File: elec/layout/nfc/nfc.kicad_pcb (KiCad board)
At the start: 2 copper layers, 40 x 40 mm, 0 parts

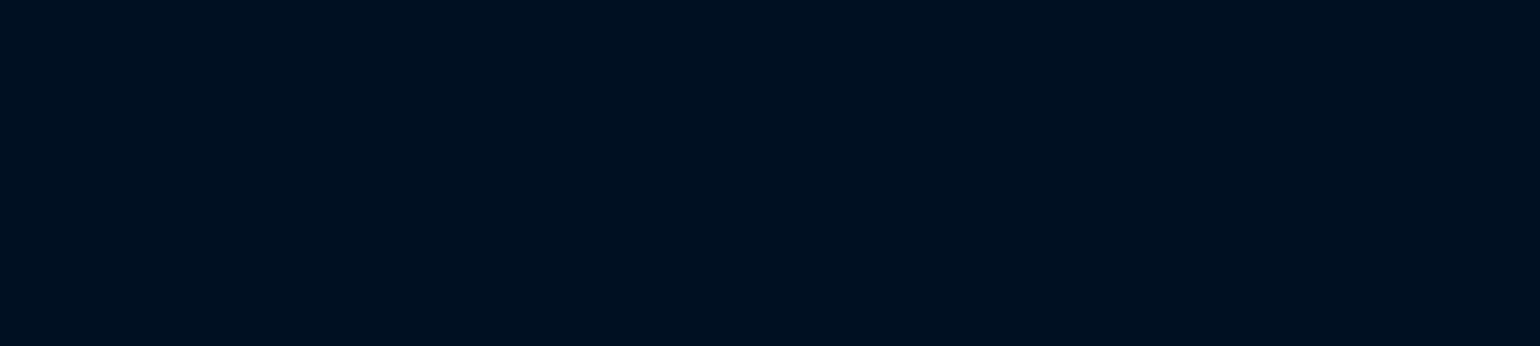
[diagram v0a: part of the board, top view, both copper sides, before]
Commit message: import copper features to hat board
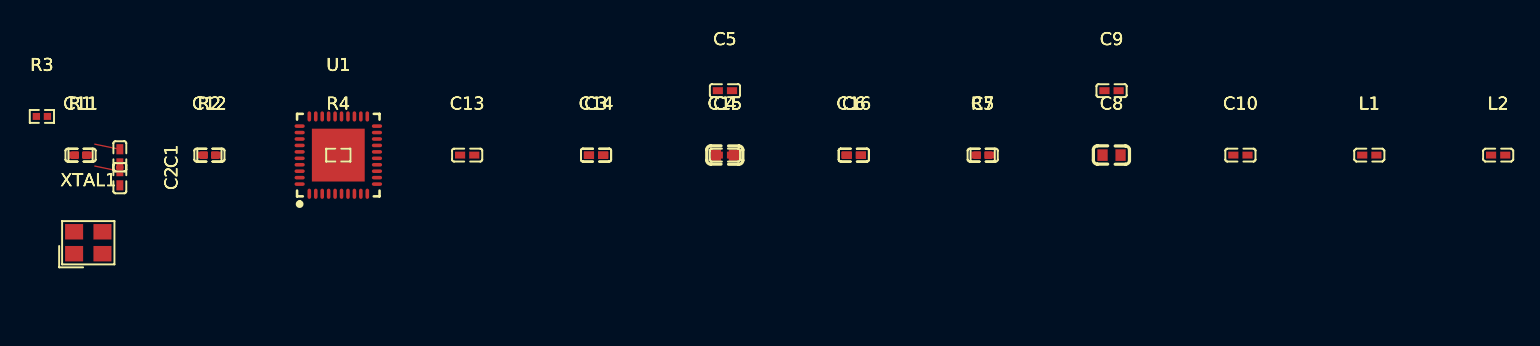
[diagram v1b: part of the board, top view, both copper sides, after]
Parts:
- added C1: , lcsc:C0402, F.Cu at (96.5, 59.7)
- added C10: , lcsc:C0402, F.Cu at (183.4, 59.6)
- added C11: 100nF ±10% 16V X7R, lcsc:C0402, F.Cu at (93.4, 59.6)
- added C12: , lcsc:C0402, F.Cu at (103.4, 59.6)
- added C13: , lcsc:C0402, F.Cu at (123.4, 59.6)
- added C14, C3: , lcsc:C0402, F.Cu at (133.4, 59.6)
- added C15: , lcsc:C0402, F.Cu at (143.4, 59.6)
- added C16, C6: , lcsc:C0402, F.Cu at (153.4, 59.6)
- added C2: , lcsc:C0402, F.Cu at (96.5, 61.4)
- added C4: 10µF ±10% 10V X5R, lcsc:C0603, F.Cu at (143.4, 59.6)
- added C5: , lcsc:C0402, F.Cu at (143.4, 54.6)
- added C7: , lcsc:C0402, F.Cu at (163.4, 59.6)
- added C8: , lcsc:C0603, F.Cu at (173.4, 59.6)
- added C9: , lcsc:C0402, F.Cu at (173.4, 54.6)
- added L1: 15nH ±5% 300mA 500mΩ, lcsc:L0402, F.Cu at (193.4, 59.6)
- added L2: , lcsc:L0402, F.Cu at (203.4, 59.6)
- added R1: 10Ω ±1% 62.5mW, lcsc:R0402, F.Cu at (93.4, 59.6)
- added R2: , lcsc:R0402, F.Cu at (103.4, 59.6)
- added R3: , lcsc:R0402, F.Cu at (90.4, 56.6)
- added R4: , lcsc:R0402, F.Cu at (113.4, 59.6)
- added R5: , lcsc:R0402, F.Cu at (163.4, 59.6)
- added U1: _NXP_Semicon_PN5321A3HN_C106_51, lcsc:QFN-40_L6.0-W6.0-P0.50-BL-EP4.1, F.Cu at (113.4, 59.6)
- added XTAL1: Crystal, lcsc:CRYSTAL-SMD_4P-L3.2-W2.5-BL, F.Cu at (94.0, 66.4)
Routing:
- net oscillator-net: track 0.00 -> 1.99 mm
- net net-6: track 0.00 -> 1.99 mm

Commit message: 50% layout for hat
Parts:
- moved C1 76.7 mm to (167.7, 88.1)
- moved C2 76.7 mm to (167.7, 89.8)
- moved C11 76.7 mm to (164.6, 88.0)
- moved R1 76.7 mm to (164.6, 88.0)
- moved R3 76.7 mm to (161.6, 85.0)
- moved XTAL1 63.9 mm to (152.6, 92.0), turned to -90 degrees
- moved U1 44.1 mm to (143.6, 91.8)
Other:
- board outline removed
- board text removed: "{{GITHASH}}"
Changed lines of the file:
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@@
 	(footprint "lcsc:C0402"
 		(layer "F.Cu")
-		(at 96.45 61.395 -90)
+		(at 167.65 89.795 -90)
 		(property "Reference" "C2"
 			(at 0 -4 -90)
@@
 	(footprint "lcsc:C0402"
 		(layer "F.Cu")
-		(at 96.45 59.695 -90)
+		(at 167.65 88.095 -90)
 		(property "Reference" "C1"
 			(at 0 -4 -90)
@@
 	(footprint "lcsc:QFN-40_L6.0-W6.0-P0.50-BL-EP4.1"
 		(layer "F.Cu")
-		(at 113.4 59.6)
+		(at 143.6 91.8)
 		(property "Reference" "U1"
 			(at 0 -7 0)
@@
 	(footprint "lcsc:R0402"
 		(layer "F.Cu")
-		(at 93.4 59.6)
+		(at 164.6 88)
 		(property "Reference" "R1"
 			(at 0 -4 0)
@@
 	(footprint "lcsc:CRYSTAL-SMD_4P-L3.2-W2.5-BL"
 		(layer "F.Cu")
-		(at 94 66.4)
+		(at 152.6 92 -90)
 		(property "Reference" "XTAL1"
-			(at 0 -4.85 0)
+			(at 0 -4.85 90)
 			(layer "F.SilkS")
 			(effects
@@
 		)
 		(property "Value" "Crystal"
-			(at 0 4.85 0)
+			(at 0 4.85 90)
 			(layer "F.Fab")
 			(effects
@@
 		)
 		(property "Footprint" ""
-			(at 0 0 0)
+			(at 0 0 90)
 			(layer "F.Fab")
 			(hide yes)
@@
 		)
 		(property "Datasheet" ""
-			(at 0 0 0)
+			(at 0 0 90)
 			(layer "F.Fab")
 			(hide yes)
@@
 		)
 		(property "Description" ""
-			(at 0 0 0)
+			(at 0 0 90)
 			(layer "F.Fab")
 			(hide yes)
@@
 		)
 		(property "atopile_address" "oscillator.crystal"
-			(at 0 0 0)
+			(at 0 0 90)
 			(layer "User.9")
 			(hide yes)
@@
 		)
 		(property "LCSC" "C70591"
-			(at 0 0 0)
+			(at 0 0 90)
 			(layer "User.9")
 			(hide yes)
@@
 		(attr smd)
 		(fp_line
-			(start -2.26 0.25)
-			(end -2.26 1.91)
+			(start -2.26 1.91)
+			(end -0.4 1.91)
 			(stroke
 				(width 0.15)
@@
 		)
 		(fp_line
-			(start -2.26 1.91)
-			(end -0.4 1.91)
+			(start -2.03 1.68)
+			(end -2.03 -1.68)
 			(stroke
 				(width 0.15)
@@
 		)
 		(fp_line
-			(start -2.03 -1.68)
-			(end 2.03 -1.68)
+			(start 2.03 1.68)
+			(end -2.03 1.68)
 			(stroke
 				(width 0.15)
@@
 		)
 		(fp_line
-			(start -2.03 1.68)
-			(end -2.03 -1.68)
+			(start -2.26 0.25)
+			(end -2.26 1.91)
 			(stroke
 				(width 0.15)
@@
 		)
 		(fp_line
-			(start 2.03 -1.68)
-			(end 2.03 1.68)
+			(start -2.03 -1.68)
+			(end 2.03 -1.68)
 			(stroke
 				(width 0.15)
@@
 		)
 		(fp_line
-			(start 2.03 1.68)
-			(end -2.03 1.68)
+			(start 2.03 -1.68)
+			(end 2.03 1.68)
 			(stroke
 				(width 0.15)
@@
 		)
 		(fp_text user "${REFERENCE}"
-			(at 0 -4.85 0)
+			(at 0 -4.85 90)
 			(layer "F.SilkS")
 			(effects
@@
 		)
 		(fp_text user "${REFERENCE}"
-			(at 0 0 0)
+			(at 0 0 90)
 			(layer "F.Fab")
 			(effects
@@
 		)
 		(fp_text user "FBRK:autoplaced"
-			(at 0 0 0)
+			(at 0 0 90)
 			(layer "User.5")
 			(effects
@@
 		)
 		(pad "1" smd rect
-			(at -1.1 0.85)
+			(at -1.1 0.85 270)
 			(size 1.4 1.2)
 			(layers "F.Cu" "F.Paste" "F.Mask")
@@
 		)
 		(pad "2" smd rect
-			(at 1.1 0.85)
+			(at 1.1 0.85 270)
 			(size 1.4 1.2)
 			(layers "F.Cu" "F.Paste" "F.Mask")
@@
 		)
 		(pad "3" smd rect
-			(at 1.1 -0.85)
+			(at 1.1 -0.85 270)
 			(size 1.4 1.2)
 			(layers "F.Cu" "F.Paste" "F.Mask")
@@
 		)
 		(pad "4" smd rect
-			(at -1.1 -0.85)
+			(at -1.1 -0.85 270)
 			(size 1.4 1.2)
 			(layers "F.Cu" "F.Paste" "F.Mask")
@@
 	(footprint "lcsc:C0402"
 		(layer "F.Cu")
-		(at 93.4 59.6)
+		(at 164.6 88)
 		(property "Reference" "C11"
 			(at 0 -4 0)
@@
 	(footprint "lcsc:R0402"
 		(layer "F.Cu")
-		(at 90.4 56.6)
+		(at 161.6 85)
 		(property "Reference" "R3"
 			(at 0 -4 0)
@@
 		)
 	)
-	(gr_circle
-		(center 133.352 82.11)
-		(end 135.052 82.11)
-		(stroke
-			(width 0.1)
-			(type solid)
-		)
-		(fill none)
-		(layer "Edge.Cuts")
-	)
-	(gr_circle
-		(center 165.352 114.11)
-		(end 167.052 114.11)
-		(stroke
-			(width 0.1)
-			(type solid)
-		)
-		(fill none)
-		(layer "Edge.Cuts")
-	)
-	(gr_circle
-		(center 165.352 82.11)
-		(end 167.052 82.11)
-		(stroke
-			(width 0.1)
-			(type solid)
-		)
-		(fill none)
-		(layer "Edge.Cuts")
-	)
-	(gr_arc
-		(start 169.352 114.11)
-		(mid 168.180427 116.938427)
-		(end 165.352 118.11)
-		(stroke
-			(width 0.1)
-			(type solid)
-		)
-		(layer "Edge.Cuts")
-	)
-	(gr_arc
-		(start 133.352 118.11)
-		(mid 130.523573 116.938427)
-		(end 129.352 114.11)
-		(stroke
-			(width 0.1)
-			(type solid)
-		)
-		(layer "Edge.Cuts")
-	)
-	(gr_line
-		(start 169.352 114.11)
-		(end 169.352 82.11)
-		(stroke
-			(width 0.1)
-			(type solid)
-		)
-		(layer "Edge.Cuts")
-	)
-	(gr_line
-		(start 129.352 82.11)
-		(end 129.352 114.11)
-		(stroke
-			(width 0.1)
-			(type solid)
-		)
-		(layer "Edge.Cuts")
-	)
-	(gr_arc
-		(start 165.352 78.11)
-		(mid 168.180427 79.281573)
-		(end 169.352 82.11)
-		(stroke
-			(width 0.1)
-			(type solid)
-		)
-		(layer "Edge.Cuts")
-	)
-	(gr_line
-		(start 165.352 78.11)
-		(end 133.352 78.11)
-		(stroke
-			(width 0.1)
-			(type solid)
-		)
-		(layer "Edge.Cuts")
-	)
-	(gr_arc
-		(start 129.352 82.11)
-		(mid 130.523573 79.281573)
-		(end 133.352 78.11)
-		(stroke
-			(width 0.1)
-			(type solid)
-		)
-		(layer "Edge.Cuts")
-	)
-	(gr_circle
-		(center 133.352 114.11)
-		(end 135.052 114.11)
-		(stroke
-			(width 0.1)
-			(type solid)
-		)
-		(fill none)
-		(layer "Edge.Cuts")
-	)
-	(gr_line
-		(start 133.352 118.11)
-		(end 165.352 118.11)
-		(stroke
-			(width 0.1)
-			(type solid)
-		)
-		(layer "Edge.Cuts")
-	)
-	(gr_text "{{GITHASH}}"
-		(at 140.240427 116.111573 0)
-		(layer "F.SilkS")
-		(effects
-			(font
-				(size 2 2)
-				(thickness 0.1)
-			)
-			(justify left bottom)
-		)
-	)
 	(segment
-		(start 96.45 59.15)
-		(end 94.5 58.75)
+		(start 167.65 87.55)
+		(end 165.7 87.15)
 		(width 0.1)
 		(layer "F.Cu")
@@
 	)
 	(segment
-		(start 96.45 60.85)
-		(end 94.5 60.45)
+		(start 167.65 89.25)
+		(end 165.7 88.85)
 		(width 0.1)
 		(layer "F.Cu")
 		(net 4)
 	)
-	(group ""
-		(members "019c0a6d-9bb8-42f8-8584-8f200b71a27b" "097c55d3-ce7a-4886-a7db-9a4e9fcd0127"
-			"0e8e5788-23b0-4e0e-993f-a94957498ae3" "178364bc-250e-4a39-b0ba-4262bbac4b46"
-			"3d8baf97-c836-4397-867c-23e52ff05ce1" "871dfad9-a85d-42ce-9d2d-6520fae7f4c4"
-			"8baef1cd-8e58-474a-b843-199aa0080763" "a7e36be5-cc10-4aad-836f-bde309666136"
-			"b80e33ff-046b-4986-bc0d-6bc4865afc31" "cf226ff4-3173-434d-8c9b-3129470c1ce4"
-			"d6648504-8f45-4127-8704-34acfec9c9a4" "e1f36007-0f9d-4dc5-ae43-6b056652526f"
-		)
-	)
 )

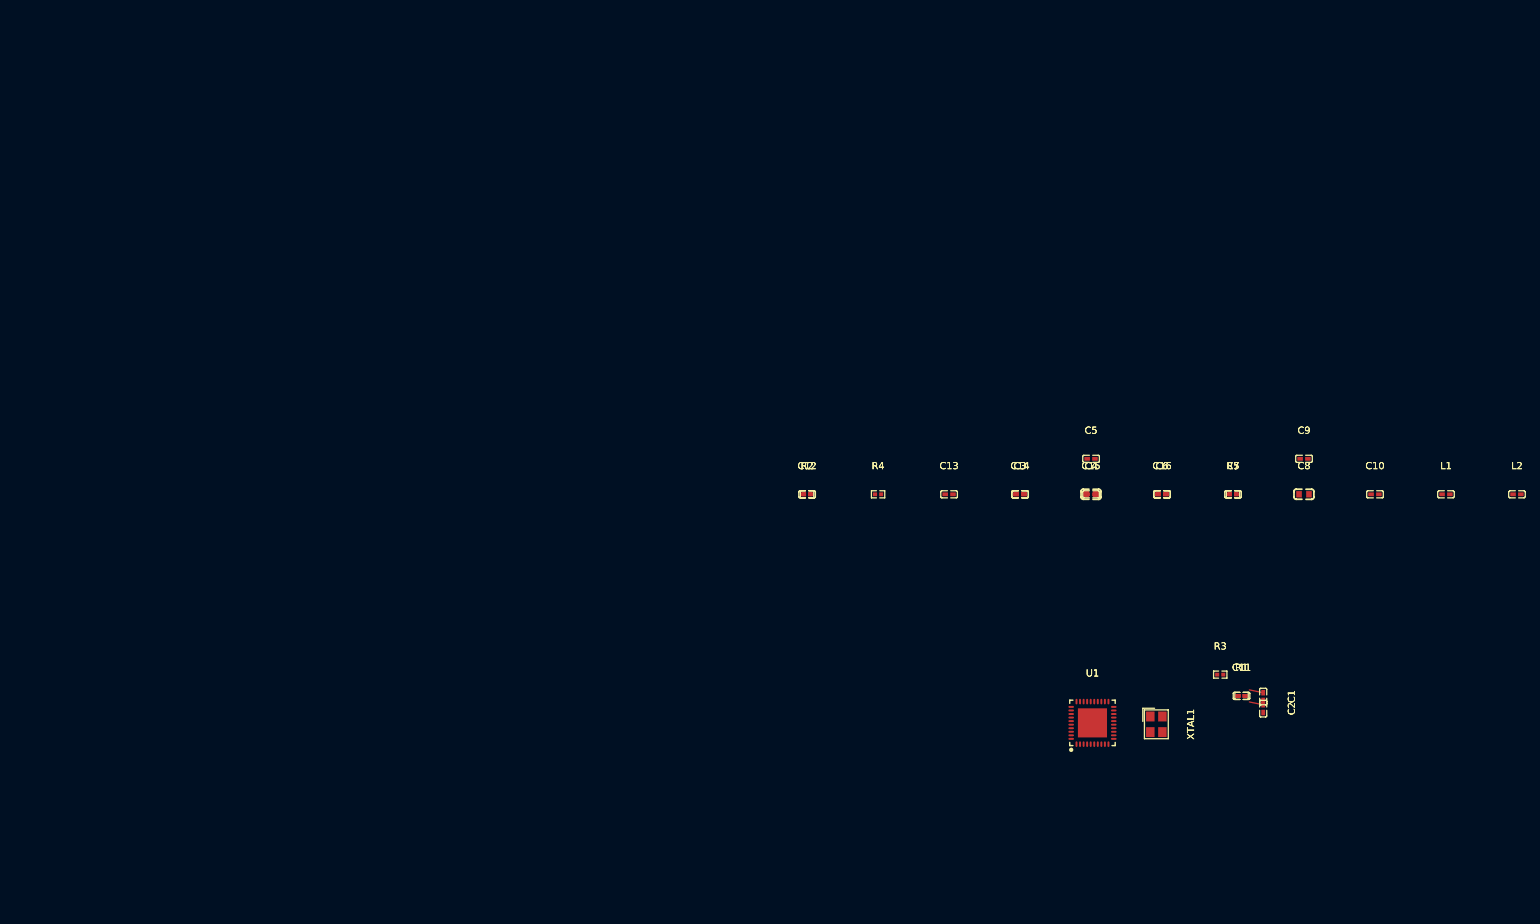
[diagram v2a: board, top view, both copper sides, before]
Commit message: layout NFC module
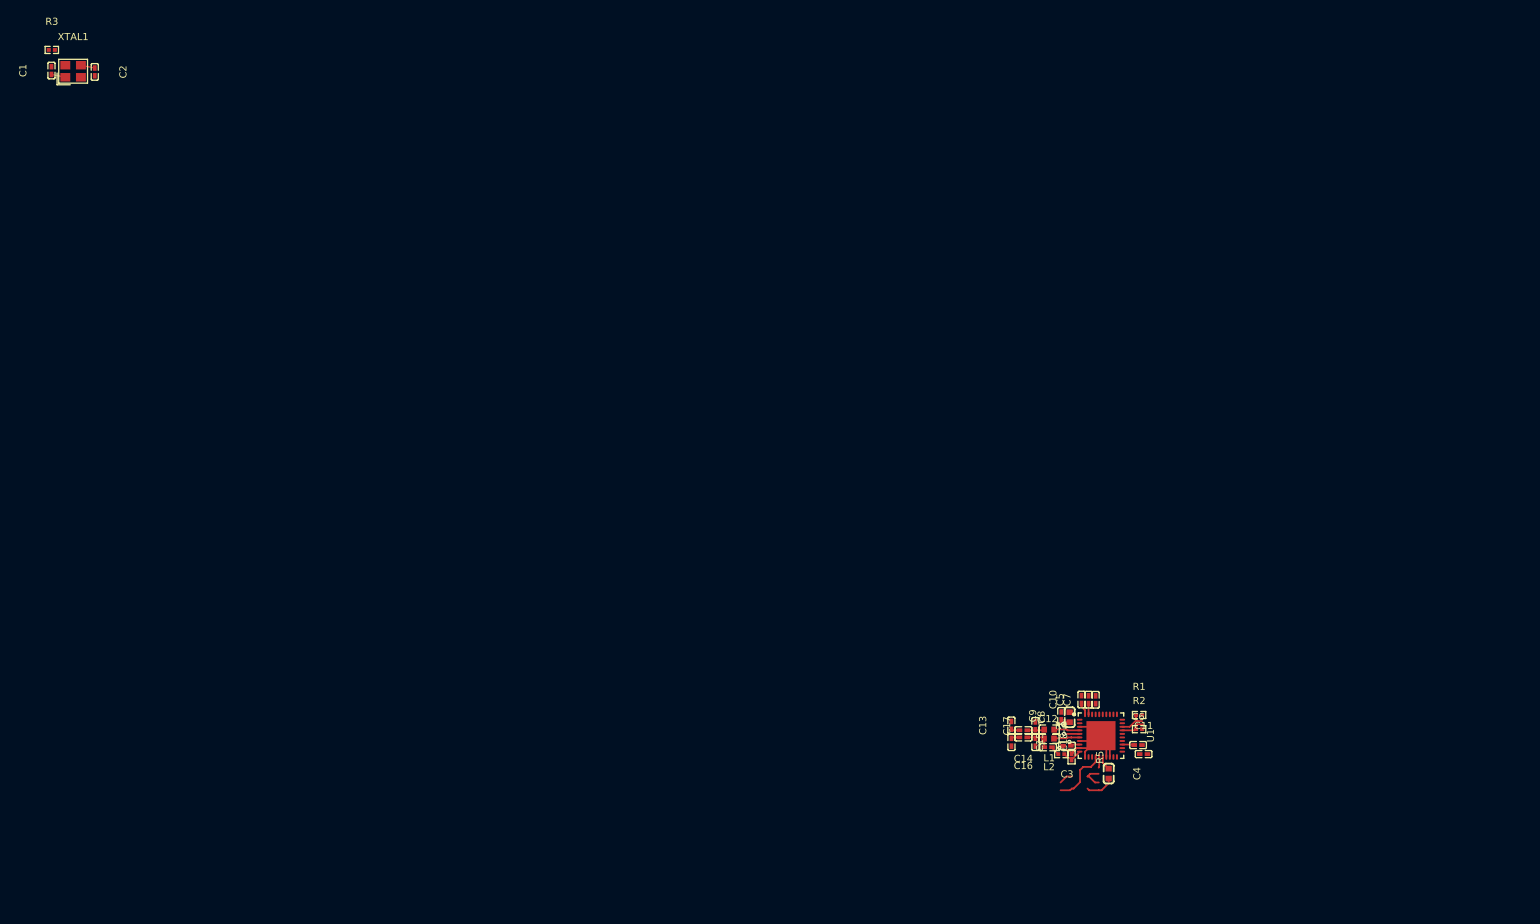
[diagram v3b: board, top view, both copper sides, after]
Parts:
- added C17: 220pF ±10% 50V X7R, lcsc:C0402, F.Cu at (135.6, 92.2)
- added C18: , lcsc:C0402, F.Cu at (135.6, 94.5)
- C13: value (none) -> 100pF ±5% 50V C0G
- C14: value (none) -> 20pF ±5% 50V C0G
- L1: value 15nH ±5% 300mA 500mΩ -> 560nH ±5% 450mA 480mΩ; footprint lcsc:L0402 -> lcsc:IND-SMD_L1.6-W0.8-1
- L2: footprint lcsc:L0402 -> lcsc:IND-SMD_L1.6-W0.8-1
- R4: value (none) -> 1kΩ ±1% 62.5mW
- moved C1 192.1 mm to (-3.05, -0.10), turned to 90 degrees
- moved C2 187.5 mm to (3.05, 0.10)
- moved R3 186.6 mm to (-3.00, -3.00)
- moved XTAL1 178.2 mm to (0.00, 0.00), turned to 0 degrees
- moved L2 74.4 mm to (137.5, 94.0), turned to 180 degrees
- moved L1 65.0 mm to (137.5, 92.7), turned to 180 degrees
- moved R2 57.3 mm to (150.2, 92.7)
- moved C10 50.5 mm to (142.1, 88.5), turned to 90 degrees
- moved C9 49.8 mm to (139.2, 90.8), turned to 90 degrees
- moved C12 49.2 mm to (137.4, 95.2)
- moved C8 45.6 mm to (140.4, 91.0), turned to 90 degrees
- moved R4 44.8 mm to (139.2, 96.2)
- moved R5 43.5 mm to (140.7, 96.6), turned to -90 degrees
- moved C16 39.4 mm to (133.9, 93.8), turned to 180 degrees
- moved C4 39.4 mm to (145.9, 98.9), turned to -90 degrees
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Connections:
- C1 pad 2: net-1 -> net-2
- C10 pad 1: net -> net-1
- C10 pad 2: net-1 -> net-2
- C11 pad 1: net-1 -> net-2
- C12 pad 2: net-10 -> net-8
- C13 pad 1: tx_1_mid -> net-6
- C13 pad 2: net-1 -> net-2
- C14 pad 2: signal-1 -> net-6
- C15 pad 1: tx_2_mid -> net-12
- C15 pad 2: net-1 -> net-2
- C16 pad 2: signal -> net-12
- C2 pad 1: net-6 -> net-3
- C2 pad 2: net-1 -> net-2
- C3 pad 1: net -> net-1
- C3 pad 2: net-1 -> net-2
- C4 pad 1: net -> net-1
- C4 pad 2: net-1 -> net-2
- C5 pad 1: net -> net-1
- C5 pad 2: net-1 -> net-2
- C6 pad 1: net -> net-1
- C6 pad 2: net-1 -> net-2
- C7 pad 1: net-4 -> net
- C8 pad 1: net -> net-1
- C8 pad 2: net-1 -> net-2
- C9 pad 1: net -> net-1
- C9 pad 2: net-1 -> net-2
- L1 pad 2: net-8 -> net-7
- R1 pad 1: net-5 -> net-4
- R2 pad 1: net-2 -> net-10
- R3 pad 2: net-3 -> net-5
- R4 pad 1: net-10 -> net-8
- R4 pad 2: net-7 -> net-11
- R5 pad 1: net-1 -> net-2
- R5 pad 2: net-7 -> net-11
- U1 pad 1: net-1 -> net-2
- U1 pad 10: net-7 -> net-11
- U1 pad 11: net-1 -> net-2
- U1 pad 14: net-6 -> net-3
- U1 pad 15: net-3 -> net-5
- U1 pad 16: net -> net-1
- U1 pad 17: net-1 -> net-2
- U1 pad 18: net-1 -> net-2
- U1 pad 23: net -> net-1
- U1 pad 27: net-2 -> net-10
- U1 pad 28: net-5 -> net-4
- U1 pad 3: net-1 -> net-2
- U1 pad 37: net-4 -> net
- U1 pad 39: net -> net-1
- U1 pad 4: net-8 -> net-7
- U1 pad 40: net -> net-1
- U1 pad 41: net-1 -> net-2
- U1 pad 5: net -> net-1
- U1 pad 7: net-1 -> net-2
- U1 pad 8: net -> net-1
- U1 pad 9: net-1 -> net-2
- XTAL1 pad 1: net-1 -> oscillator-net
- XTAL1 pad 2: net-6 -> net-2
- XTAL1 pad 3: oscillator-net -> net-3
- XTAL1 pad 4: oscillator.crystal.footprint.pins[3].net-net -> net-2
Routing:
- net net-1: track 0.00 -> 31.9 mm, vias 0 -> 1
- net net-5: track 0.00 -> 14.3 mm, vias 0 -> 3
- net net-3: track 0.00 -> 10.3 mm
- net net-8: track 0.00 -> 4.67 mm
- net net-4: track 0.00 -> 3.96 mm
- net net-10: track 0.00 -> 3.91 mm
- net tx_2_mid: track 0.00 -> 3.78 mm
- net oscillator-net: track 1.99 -> 5.66 mm
- net net-11: track 0.00 -> 3.66 mm
- net net-2: track 0.00 -> 2.75 mm
- net tx_1_mid: track 0.00 -> 2.42 mm
- net net-12: track 0.00 -> 1.57 mm
- net net-9: track 0.00 -> 1.55 mm
- net net-7: track 0.00 -> 1.20 mm
- net net-6: track 1.99 -> 1.18 mm
